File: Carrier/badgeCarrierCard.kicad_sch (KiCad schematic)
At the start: 28 parts, among them J1 USB_C_Receptacle_USB2.0_16P, J2 MDT420M02003, J3 Conn_01x08, J7 Conn_01x10, U11 TPSGM7227YUWQ10G

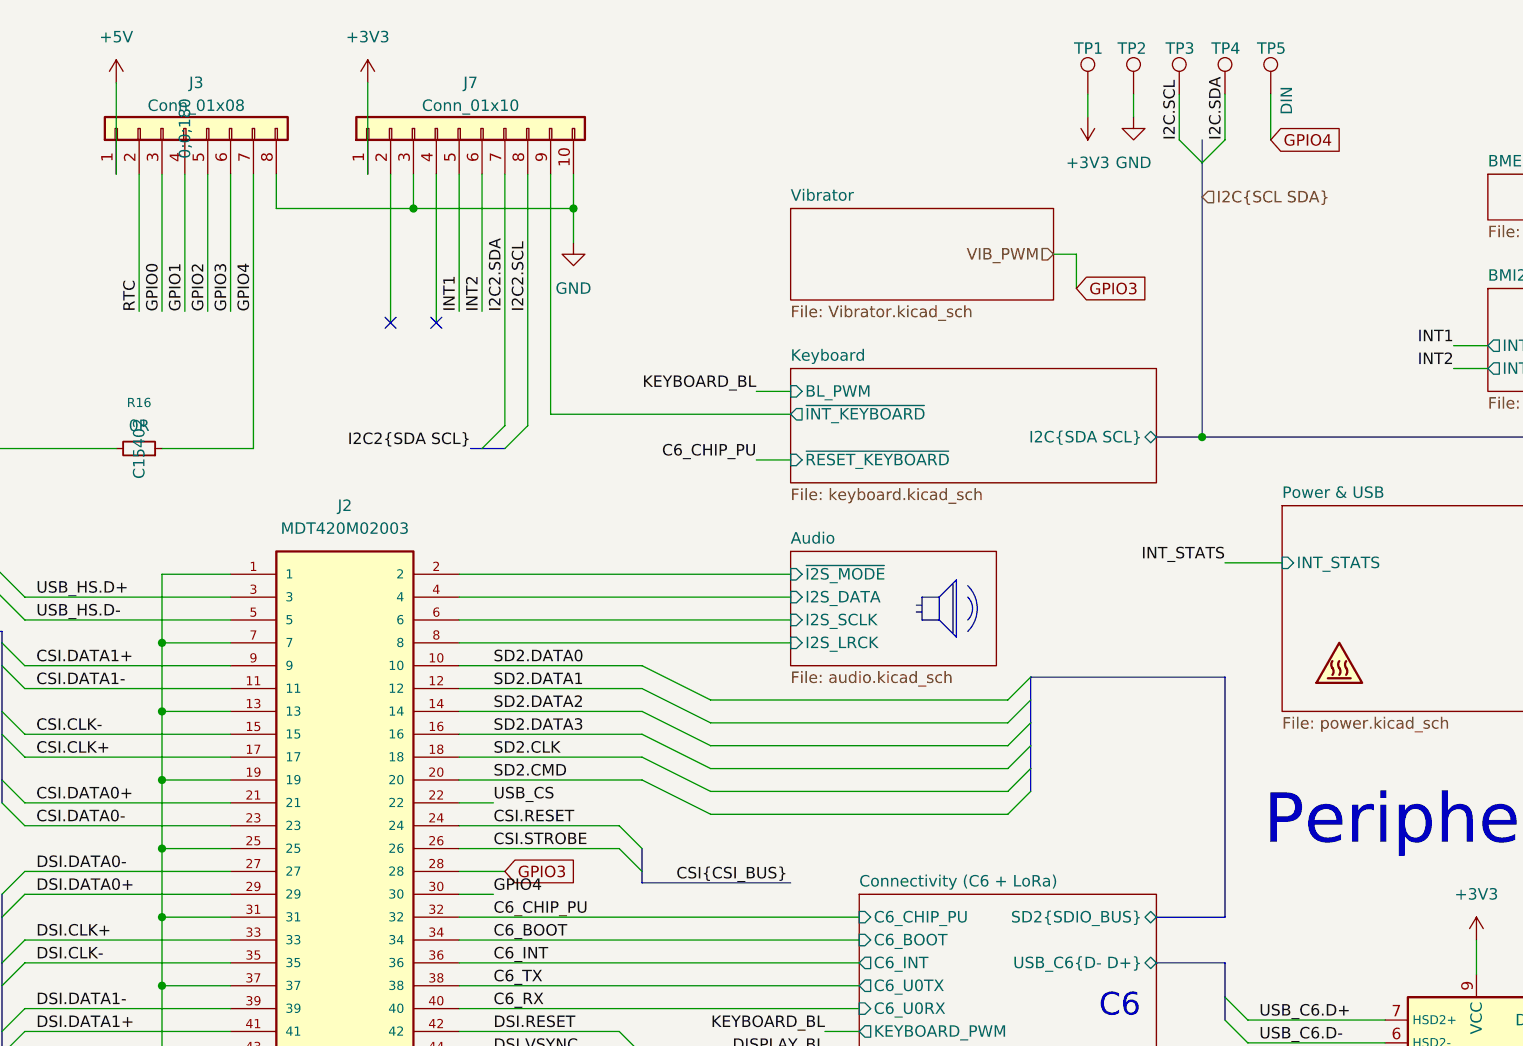
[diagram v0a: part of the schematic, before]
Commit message: fix: sync schematic prot3 and v2.5
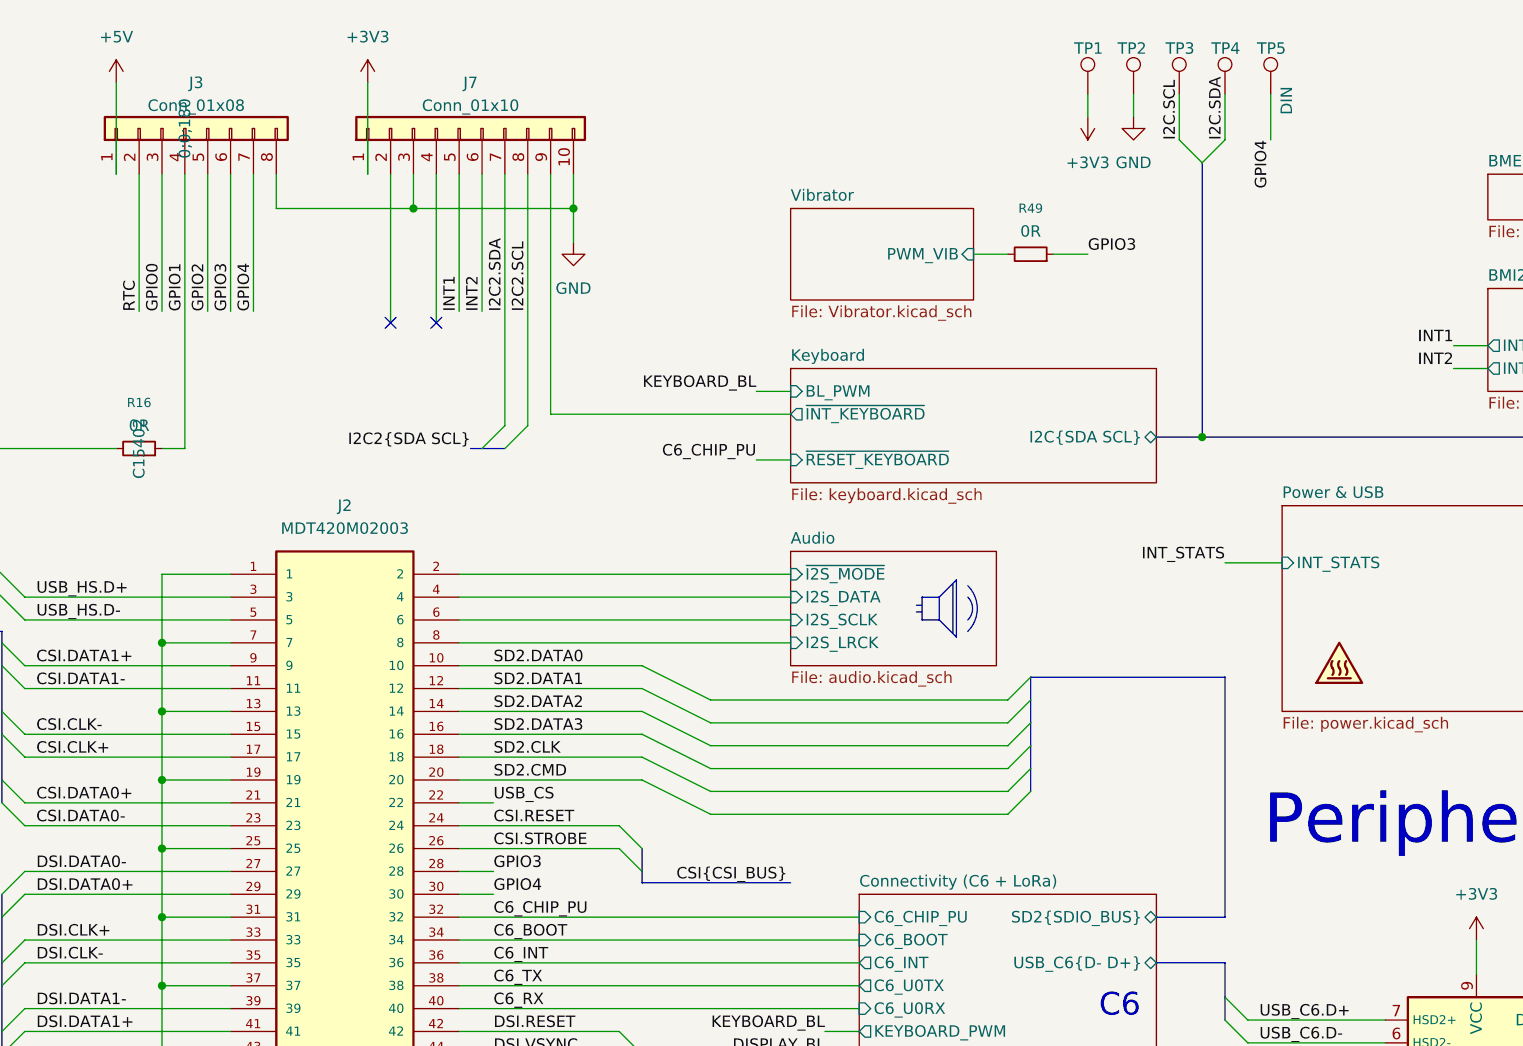
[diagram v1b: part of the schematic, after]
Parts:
- added R49: 0R, Resistor_SMD:R_0603_1608Metric, symbol Device:R_Small
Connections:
- net GPIO1: now also R16.1
- net GPIO3: now also R49.1
- net GPIO4: no longer R16.1
- new net Vibrator/PWM_VIB: R49.2
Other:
- sheet Vibrator ports: added PWM_VIB; removed none
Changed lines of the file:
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@@
 		)
 	)
-	(bus
+	(polyline
 		(pts
-			(xy 210.82 29.21) (xy 210.82 31.75)
+			(xy 28.448 100.838) (xy 28.702 101.092)
 		)
 		(stroke
@@
 		)
 	)
-	(polyline
+	(wire
 		(pts
-			(xy 28.448 100.838) (xy 28.702 101.092)
+			(xy 95.25 115.57) (xy 102.87 115.57)
 		)
 		(stroke
@@
 		)
 	)
-	(wire
+	(polyline
 		(pts
-			(xy 95.25 115.57) (xy 102.87 115.57)
+			(xy 33.274 98.552) (xy 34.29 98.552)
 		)
 		(stroke
@@
 		)
 	)
-	(polyline
+	(wire
 		(pts
-			(xy 33.274 98.552) (xy 34.29 98.552)
+			(xy 185.42 41.91) (xy 189.23 41.91)
 		)
 		(stroke
@@
 		)
 	)
+	(wire
+		(pts
+			(xy 198.12 41.91) (xy 194.31 41.91)
+		)
+		(stroke
+			(width 0)
+			(type default)
+		)
+	)
 	(polyline
 		(pts
@@
 		)
 	)
-	(wire
-		(pts
-			(xy 95.25 63.5) (xy 105.41 63.5)
-		)
-		(stroke
-			(width 0)
-			(type default)
-		)
-	)
 	(bus
 		(pts
@@
 	(wire
 		(pts
+			(xy 105.41 33.02) (xy 105.41 48.26)
+		)
+		(stroke
+			(width 0)
+			(type default)
+		)
+	)
+	(wire
+		(pts
 			(xy 149.86 139.7) (xy 157.48 139.7)
 		)
@@
 	(wire
 		(pts
+			(xy 95.25 63.5) (xy 97.79 63.5)
+		)
+		(stroke
+			(width 0)
+			(type default)
+		)
+	)
+	(wire
+		(pts
 			(xy 19.05 63.5) (xy 19.05 115.57)
 		)
@@
 	(wire
 		(pts
-			(xy 194.31 41.91) (xy 196.85 41.91)
-		)
-		(stroke
-			(width 0)
-			(type default)
-		)
-	)
-	(wire
-		(pts
 			(xy 48.26 163.83) (xy 48.26 166.37)
 		)
@@
 	(wire
 		(pts
-			(xy 128.27 110.49) (xy 133.35 110.49)
+			(xy 128.27 110.49) (xy 132.08 110.49)
 		)
 		(stroke
@@
 	(wire
 		(pts
-			(xy 97.79 33.02) (xy 97.79 48.26)
+			(xy 97.79 33.02) (xy 97.79 63.5)
 		)
 		(stroke
@@
 	(wire
 		(pts
-			(xy 105.41 33.02) (xy 105.41 63.5)
-		)
-		(stroke
-			(width 0)
-			(type default)
-		)
-	)
-	(wire
-		(pts
-			(xy 196.85 41.91) (xy 196.85 45.72)
-		)
-		(stroke
-			(width 0)
-			(type default)
-		)
-	)
-	(wire
-		(pts
 			(xy 80.01 110.49) (xy 102.87 110.49)
 		)
@@
 		)
 	)
+	(label "GPIO3"
+		(at 198.12 41.91 0)
+		(effects
+			(font
+				(size 1.27 1.27)
+			)
+			(justify left bottom)
+		)
+	)
 	(label "I2C2.SCL"
 		(at 132.08 140.97 0)
@@
 		)
 	)
+	(label "GPIO3"
+		(at 132.08 110.49 0)
+		(effects
+			(font
+				(size 1.27 1.27)
+			)
+			(justify left bottom)
+		)
+	)
 	(label "GPIO2"
 		(at 100.33 48.26 90)
@@
 		)
 	)
-	(label "CSI{CSI_BUS}"
-		(at 63.5 83.82 0)
-		(effects
-			(font
-				(size 1.27 1.27)
-			)
-			(justify left bottom)
-		)
-	)
-	(global_label "GPIO3"
-		(shape input)
-		(at 196.85 45.72 0)
-		(fields_autoplaced yes)
-		(effects
-			(font
-				(size 1.27 1.27)
-			)
-			(justify left)
-		)
-		(property "Intersheetrefs" "${INTERSHEET_REFS}"
-			(at 205.52 45.72 0)
-			(effects
-				(font
-					(size 1.27 1.27)
-				)
-				(justify left)
-				(hide yes)
-			)
-		)
-	)
-	(global_label "GPIO3"
-		(shape input)
-		(at 133.35 110.49 0)
-		(fields_autoplaced yes)
-		(effects
-			(font
-				(size 1.27 1.27)
-			)
-			(justify left)
-		)
-		(property "Intersheetrefs" "${INTERSHEET_REFS}"
-			(at 142.02 110.49 0)
-			(effects
-				(font
-					(size 1.27 1.27)
-				)
-				(justify left)
-				(hide yes)
-			)
-		)
-	)
-	(global_label "GPIO4"
-		(shape input)
-		(at 218.44 29.21 0)
-		(fields_autoplaced yes)
-		(effects
-			(font
-				(size 1.27 1.27)
-			)
-			(justify left)
-		)
-		(property "Intersheetrefs" "${INTERSHEET_REFS}"
-			(at 227.11 29.21 0)
-			(effects
-				(font
-					(size 1.27 1.27)
-				)
-				(justify left)
-				(hide yes)
-			)
-		)
-	)
-	(hierarchical_label "I2C{SCL SDA}"
-		(shape input)
-		(at 210.82 35.56 0)
+	(label "GPIO4"
+		(at 218.44 29.21 270)
 		(effects
 			(font
 				(size 1.27 1.27)
 			)
-			(justify left)
+			(justify right bottom)
 		)
 	)
-	(hierarchical_label "VIB_PWM"
-		(shape input)
-		(at 194.31 41.91 180)
+	(label "CSI{CSI_BUS}"
+		(at 63.5 83.82 0)
 		(effects
 			(font
 				(size 1.27 1.27)
 			)
-			(justify right)
+			(justify left bottom)
 		)
 	)
@@
 	)
 	(symbol
+		(lib_id "Device:R_Small")
+		(at 191.77 41.91 270)
+		(mirror x)
+		(unit 1)
+		(exclude_from_sim no)
+		(in_bom yes)
+		(on_board yes)
+		(dnp no)
+		(property "Reference" "R49"
+			(at 191.77 36.83 90)
+			(effects
+				(font
+					(size 1.016 1.016)
+				)
+			)
+		)
+		(property "Value" "0R"
+			(at 191.77 39.37 90)
+			(effects
+				(font
+					(size 1.27 1.27)
+				)
+			)
+		)
+		(property "Footprint" "Resistor_SMD:R_0603_1608Metric"
+			(at 191.77 41.91 0)
+			(effects
+				(font
+					(size 1.27 1.27)
+				)
+				(hide yes)
+			)
+		)
+		(property "Datasheet" "~"
+			(at 191.77 41.91 0)
+			(effects
+				(font
+					(size 1.27 1.27)
+				)
+				(hide yes)
+			)
+		)
+		(property "Description" "Resistor, small symbol"
+			(at 191.77 41.91 0)
+			(effects
+				(font
+					(size 1.27 1.27)
+				)
+				(hide yes)
+			)
+		)
+		(property "LCSC" "C15402"
+			(at 183.642 48.006 0)
+			(effects
+				(font
+					(size 1.27 1.27)
+				)
+				(hide yes)
+			)
+		)
+		(property "DigiKey_Part_Number" ""
+			(at 191.77 41.91 0)
+			(effects
+				(font
+					(size 1.27 1.27)
+				)
+			)
+		)
+		(property "Sim.Pin" ""
+			(at 191.77 41.91 0)
+			(effects
+				(font
+					(size 1.27 1.27)
+				)
+			)
+		)
+		(property "JLCPCB_CORRECTION" ""
+			(at 191.77 41.91 0)
+			(effects
+				(font
+					(size 1.27 1.27)
+				)
+			)
+		)
+		(pin "2"
+		)
+		(pin "1"
+		)
+		(instances
+			(project "badgeCarrierCard"
+				(path "/d0a98fce-b133-4503-8f8a-83b2a1eed591"
+					(reference "R49")
+					(unit 1)
+				)
+			)
+		)
+	)
+	(symbol
 		(lib_id "Connector_Generic:Conn_01x08")
 		(at 97.79 27.94 90)
@@
 	(sheet
 		(at 165.1 36.83)
-		(size 29.21 10.16)
+		(size 20.32 10.16)
 		(exclude_from_sim no)
 		(in_bom yes)
@@
 			)
 		)
+		(pin "PWM_VIB" input
+			(at 185.42 41.91 0)
+			(effects
+				(font
+					(size 1.27 1.27)
+				)
+				(justify right)
+			)
+		)

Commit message: push final
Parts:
- R49: footprint Resistor_SMD:R_0603_1608Metric -> Resistor_SMD:R_0402_1005Metric
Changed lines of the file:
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@@
 			)
 		)
-		(property "Footprint" "Resistor_SMD:R_0603_1608Metric"
+		(property "Footprint" "Resistor_SMD:R_0402_1005Metric"
 			(at 191.77 41.91 0)
 			(effects

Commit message: fix: add ordercodes for production files
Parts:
- R49: LCSC C15402 -> C17168
- TP1, TP2, TP3, TP4, TP5: now left out of the parts list

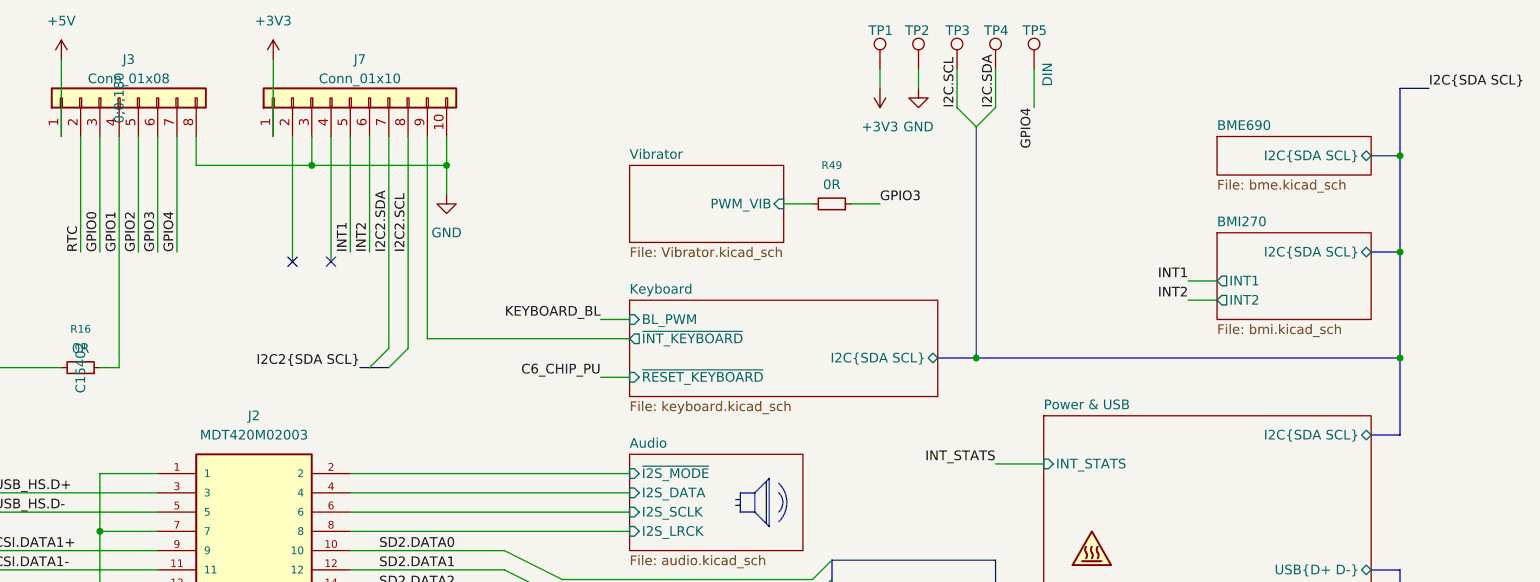
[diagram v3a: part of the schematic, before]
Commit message: fix: cleanup silkscreen labels
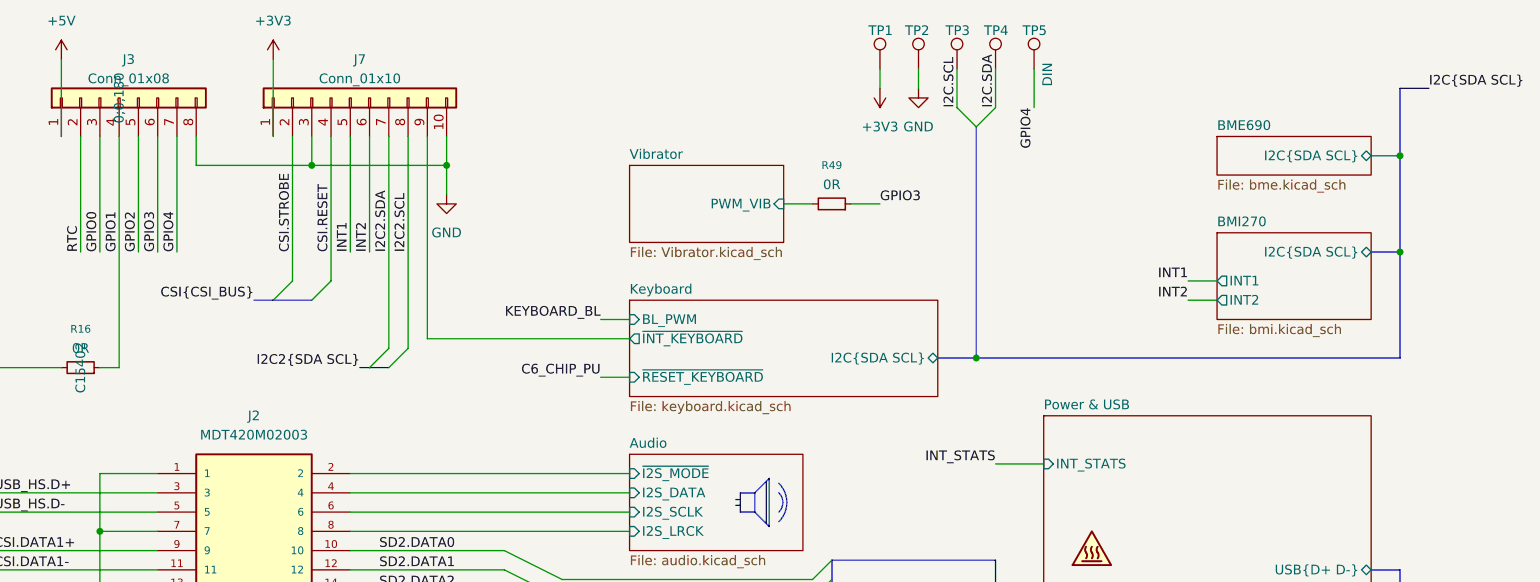
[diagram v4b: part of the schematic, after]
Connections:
- net CSI.RESET: now also J7.4 (Pin_4)
- net CSI.STROBE: now also J7.2 (Pin_2)
- no-connect marks 8 -> 6
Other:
- sheet Power & USB ports: added none; removed I2C{SDA SCL}
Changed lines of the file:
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@@
 	)
 	(junction
-		(at 266.7 62.23)
-		(diameter 0)
-		(color 0 0 0 0)
-	)
-	(junction
 		(at 55.88 181.61)
 		(diameter 0)
@@
 	)
 	(no_connect
-		(at 125.73 49.53)
-	)
-	(no_connect
 		(at 99.06 146.05)
 	)
@@
 	)
 	(no_connect
-		(at 120.65 49.53)
-	)
-	(no_connect
 		(at 48.26 179.07)
 	)
@@
 	)
 	(bus_entry
+		(at 123.19 54.61)
+		(size 2.54 -2.54)
+		(stroke
+			(width 0)
+			(type default)
+		)
+	)
+	(bus_entry
 		(at 210.82 31.75)
 		(size -2.54 -2.54)
@@
 	)
 	(bus_entry
+		(at 118.11 54.61)
+		(size 2.54 -2.54)
+		(stroke
+			(width 0)
+			(type default)
+		)
+	)
+	(bus_entry
 		(at 77.47 128.27)
 		(size 2.54 -2.54)
@@
 	(wire
 		(pts
-			(xy 125.73 33.02) (xy 125.73 49.53)
-		)
-		(stroke
-			(width 0)
-			(type default)
-		)
-	)
-	(wire
-		(pts
 			(xy 81.915 178.435) (xy 81.915 179.705)
 		)
@@
 	(bus
 		(pts
+			(xy 115.57 54.61) (xy 118.11 54.61)
+		)
+		(stroke
+			(width 0)
+			(type default)
+		)
+	)
+	(bus
+		(pts
 			(xy 270.51 26.67) (xy 266.7 26.67)
 		)
@@
 	(bus
 		(pts
-			(xy 262.89 72.39) (xy 266.7 72.39)
-		)
-		(stroke
-			(width 0)
-			(type default)
-		)
-	)
-	(bus
-		(pts
 			(xy 58.42 88.9) (xy 58.42 93.98)
 		)
@@
 		)
 	)
-	(bus
-		(pts
-			(xy 266.7 72.39) (xy 266.7 62.23)
-		)
-		(stroke
-			(width 0)
-			(type default)
-		)
-	)
 	(polyline
 		(pts
@@
 	(bus
 		(pts
+			(xy 123.19 54.61) (xy 118.11 54.61)
+		)
+		(stroke
+			(width 0)
+			(type default)
+		)
+	)
+	(bus
+		(pts
 			(xy 191.77 99.06) (xy 191.77 101.6)
 		)
@@
 	(wire
 		(pts
-			(xy 120.65 33.02) (xy 120.65 49.53)
-		)
-		(stroke
-			(width 0)
-			(type default)
-		)
-	)
-	(wire
-		(pts
 			(xy 218.44 24.13) (xy 218.44 29.21)
 		)
@@
 	(wire
 		(pts
+			(xy 120.65 33.02) (xy 120.65 52.07)
+		)
+		(stroke
+			(width 0)
+			(type default)
+		)
+	)
+	(wire
+		(pts
 			(xy 128.27 107.95) (xy 146.05 107.95)
 		)
@@
 	(wire
 		(pts
+			(xy 125.73 33.02) (xy 125.73 52.07)
+		)
+		(stroke
+			(width 0)
+			(type default)
+		)
+	)
+	(wire
+		(pts
 			(xy 161.29 57.15) (xy 165.1 57.15)
 		)
@@
 		)
 	)
+	(label "CSI{CSI_BUS}"
+		(at 115.57 54.61 180)
+		(effects
+			(font
+				(size 1.27 1.27)
+			)
+			(justify right bottom)
+		)
+	)
 	(label "USB_JTAG{D+ D-}"
 		(at 73.66 161.29 90)
@@
 		)
 	)
+	(label "CSI.RESET"
+		(at 125.73 48.26 90)
+		(effects
+			(font
+				(size 1.27 1.27)
+			)
+			(justify left bottom)
+		)
+	)
 	(label "I2C2.SCL"
 		(at 132.08 140.97 0)
@@
 		)
 	)
+	(label "CSI.STROBE"
+		(at 120.65 48.26 90)
+		(effects
+			(font
+				(size 1.27 1.27)
+			)
+			(justify left bottom)
+		)
+	)
 	(hierarchical_label "I2C{SDA SCL}"
 		(shape bidirectional)
@@
 			)
 		)
-		(pin "I2C{SDA SCL}" bidirectional
-			(at 262.89 72.39 0)
-			(effects
-				(font
-					(size 1.27 1.27)
-				)
-				(justify right)
-			)
-		)
